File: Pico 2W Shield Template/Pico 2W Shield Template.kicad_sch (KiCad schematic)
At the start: 3 parts, among them J1 Socket_1x20_P2.54mm, J2 Socket_1x20_P2.54mm

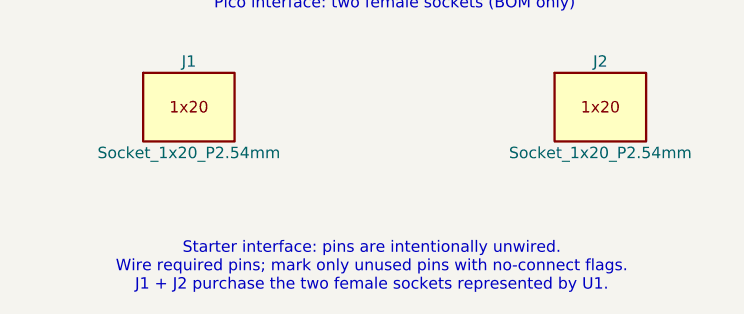
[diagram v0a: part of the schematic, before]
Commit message: Add headers to shield template
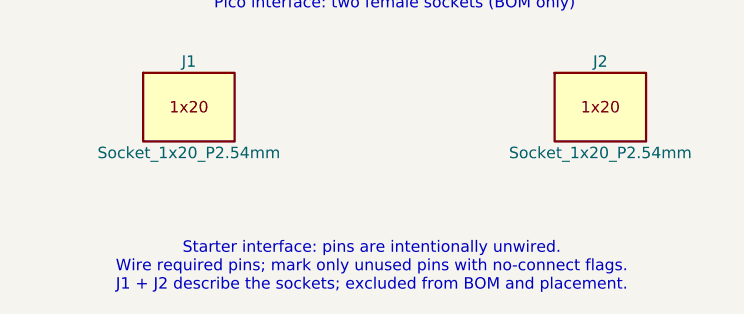
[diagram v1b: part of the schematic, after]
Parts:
- J1, J2: now left out of the parts list
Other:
- note added: "Starter interface: pins are intentionally unwired. Wire required pins; mark only unused pins with no-connect flags. J1 + J2 describe the sockets; excluded from BOM and placement."
- note removed: "Starter interface: pins are intentionally unwired. Wire required pins; mark only unused pins with no-connect flags. J1 + J2 purchase the two female sockets represented by U1."
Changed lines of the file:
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@@
 	(generator_version "10.0")
 	(paper "A4")
-	(text "Starter interface: pins are intentionally unwired.\nWire required pins; mark only unused pins with no-connect flags.\nJ1 + J2 purchase the two female sockets represented by U1."
+	(text "Starter interface: pins are intentionally unwired.\nWire required pins; mark only unused pins with no-connect flags.\nJ1 + J2 describe the sockets; excluded from BOM and placement."
 		(exclude_from_sim no)
 		(at 76.2 144.78 0)
@@
 		(body_style 1)
 		(exclude_from_sim yes)
-		(in_bom yes)
+		(in_bom no)
 		(on_board no)
 		(in_pos_files no)
@@
 			)
 		)
-		(property "Description" "Female 1x20 socket header, 2.54 mm pitch; BOM-only component for the combined Pico interface footprint"
+		(property "Description" "Female 1x20 socket header, 2.54 mm pitch; optional purchasing fields for the combined Pico interface footprint"
 			(at 55.88 127 0)
 			(hide yes)
@@
 		(body_style 1)
 		(exclude_from_sim yes)
-		(in_bom yes)
+		(in_bom no)
 		(on_board no)
 		(in_pos_files no)
@@
 			)
 		)
-		(property "Description" "Female 1x20 socket header, 2.54 mm pitch; BOM-only component for the combined Pico interface footprint"
+		(property "Description" "Female 1x20 socket header, 2.54 mm pitch; optional purchasing fields for the combined Pico interface footprint"
 			(at 101.6 127 0)
 			(hide yes)
